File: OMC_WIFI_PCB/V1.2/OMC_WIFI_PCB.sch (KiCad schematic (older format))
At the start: 20 parts, among them J1 Line Input, J10 Power, J11 Conn_01x06_Male, J12 Line Output, J13 Conn_01x06_Male, J2 Nuetral Input, J3 Neutral Output, J4 Switch, J5 Pins_FT232R, J8 Regulador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

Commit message: Actualización PCB y nueva librería para plug macho
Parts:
- removed J1: Line Input, omc-plugs:OMC-Male-Plug, symbol Connector:Conn_01x01_Male
- removed J2: Nuetral Input, omc-plugs:OMC-Male-Plug, symbol Connector:Conn_01x01_Male
- added J1: Conn_01x02_Male, omc-plugs:OMC-Male-Plug, symbol Connector:Conn_01x02_Male
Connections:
- wire segments 105 -> 106
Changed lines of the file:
@@
 	850  2300 850  6000
-$Comp
-L Connector:Conn_01x01_Male J2
-U 1 1 624922FE
-P 1150 1450
-F 0 "J2" H 1258 1631 50  0000 C CNN
-F 1 "Nuetral Input" H 1200 1406 50  0000 C CNN
-F 2 "omc-plugs:OMC-Male-Plug" H 1150 1450 50  0001 C CNN
-F 3 "~" H 1150 1450 50  0001 C CNN
-	1    1150 1450
-	1    0    0    -1
-$EndComp
 $Comp
 L RF_Module:ESP32-WROOM-32 U1
@@
 $EndComp
 $Comp
-L Connector:Conn_01x01_Male J1
-U 1 1 6246AC9C
-P 1150 1150
-F 0 "J1" H 1258 1331 50  0000 C CNN
-F 1 "Line Input" H 1258 1240 50  0000 C CNN
-F 2 "omc-plugs:OMC-Male-Plug" H 1150 1150 50  0001 C CNN
-F 3 "~" H 1150 1150 50  0001 C CNN
-	1    1150 1150
-	1    0    0    -1
-$EndComp
-$Comp
 L power:PWR_FLAG #FLG0103
 U 1 1 62597663
@@
 	1    0    0    -1
 $EndComp
+$Comp
+L Connector:Conn_01x02_Male J1
+U 1 1 62564E0F
+P 1150 1150
+F 0 "J1" H 1258 1331 50  0000 C CNN
+F 1 "Conn_01x02_Male" H 1258 1240 50  0000 C CNN
+F 2 "omc-plugs:OMC-Male-Plug" H 1150 1150 50  0001 C CNN
+F 3 "~" H 1150 1150 50  0001 C CNN
+	1    1150 1150
+	1    0    0    -1
+$EndComp
+Wire Wire Line
+	1350 1250 1350 1450
 $EndSCHEMATC

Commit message: Actualización PCB y Librerías
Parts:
- removed J10: Power, TerminalBlock:TerminalBlock_bornier-4_P5.08mm, symbol Connector:Conn_01x04_Female
- removed J12: Line Output, omc-plugs:OMC-Female-Plug, symbol Connector:Conn_01x01_Female
- removed J3: Neutral Output, omc-plugs:OMC-Female-Plug, symbol Connector:Conn_01x01_Female
- removed J9: Datos, Connector_JST:JST_XH_S4B-XH-A-1_1x04_P2.50mm_Horizontal, symbol Connector:Conn_01x04_Female
- added D2: LED, LED_SMD:LED_0603_1608Metric_Pad1.05x0.95mm_HandSolder, symbol Device:LED
- added J2: Conn_01x02_Female, omc-schematics LE:OMC-Female-Plug, symbol Connector:Conn_01x02_Female
- added R2: 330, Resistor_SMD:R_0603_1608Metric_Pad0.98x0.95mm_HandSolder, symbol Device:R
- added U2: PZEM-004T-100A, omc-schematics LE:PZEM-OO4T-100A, symbol omc-schematics:PZEM-004T-100A
- D1: footprint LED_THT:LED_D3.0mm -> LED_SMD:LED_0603_1608Metric_Pad1.05x0.95mm_HandSolder
- K1: footprint RELAY_SLA-12VDC-SL-C -> SLA-12VDC-SL-C LE:RELAY_SLA-12VDC-SL-C
- R1: footprint Resistor_SMD:R_2010_5025Metric_Pad1.40x2.65mm_HandSolder -> Resistor_SMD:R_0603_1608Metric_Pad0.98x0.95mm_HandSolder
- R3: renamed from R2; footprint Resistor_SMD:R_2010_5025Metric_Pad1.40x2.65mm_HandSolder -> Resistor_SMD:R_0603_1608Metric_Pad0.98x0.95mm_HandSolder
- renumbered D2 to D3
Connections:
- net labels added: D22_LED_G, D23_LED_R
- net labels removed: D23_LED, VN_ZMPT, VP_ACS
- wire segments 106 -> 105
- no-connect marks 29 -> 30
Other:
- note added: "LEDs"
- note added: "Regulador 3V\n"
- note removed: "LED"
- moved on the sheet: J1, J8

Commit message: Actualización PCB
Diseño casi final
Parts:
- added C1: 1u, Capacitor_SMD:C_0603_1608Metric_Pad1.08x0.95mm_HandSolder, symbol Device:C
- added J3: Conn_01x02_Male, Connector_PinHeader_2.54mm:PinHeader_1x02_P2.54mm_Vertical, symbol Connector:Conn_01x02_Male
- added R4: 10k, Resistor_SMD:R_0603_1608Metric_Pad0.98x0.95mm_HandSolder, symbol Device:R
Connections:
- net +3V: now also R4.1; no longer U1.2 (VDD)
- net CTS: now also J5.2 (Pin_2); no longer J5.5 (Pin_5)
- net D22_LED_G: now also D1.2 (A), U1.37 (IO23); no longer R1.1, U1.36 (IO22)
- net D23_LED_R: now also D2.2 (A), U1.36 (IO22); no longer R2.1, U1.37 (IO23)
- net DTR: now also J5.6 (Pin_6); no longer J5.1 (Pin_1)
- net GND: now also J5.1 (Pin_1), R1.2, R2.2, C1.2, J3.1 (Pin_1); no longer D1.1 (K), D2.1 (K), J5.6 (Pin_6)
- net RX0: now also J5.4 (Pin_4); no longer J5.3 (Pin_3)
- net TX0: now also J5.5 (Pin_5); no longer J5.2 (Pin_2)
- net VCC: now also J5.3 (Pin_3); no longer J5.4 (Pin_4)
- net BOOT: no longer names the net of U1.25 (IO0)
- net BOOT: now also J3.2 (Pin_2)
- new net: D1.1 (K), R1.1
- new net: C1.1, R4.2, U1.2 (VDD)
- new net: D2.1 (K), R2.1
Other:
- moved on the sheet: D1, D2, R1, R2
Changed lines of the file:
@@
 L Device:R R1
 U 1 1 620FCE7F
-P 5200 4100
-F 0 "R1" V 5407 4100 50  0000 C CNN
-F 1 "330" V 5316 4100 50  0000 C CNN
-F 2 "Resistor_SMD:R_0603_1608Metric_Pad0.98x0.95mm_HandSolder" V 5130 4100 50  0001 C CNN
-F 3 "~" H 5200 4100 50  0001 C CNN
-	1    5200 4100
+P 5650 4100
+F 0 "R1" V 5857 4100 50  0000 C CNN
+F 1 "330" V 5766 4100 50  0000 C CNN
+F 2 "Resistor_SMD:R_0603_1608Metric_Pad0.98x0.95mm_HandSolder" V 5580 4100 50  0001 C CNN
+F 3 "~" H 5650 4100 50  0001 C CNN
+	1    5650 4100
 	0    -1   -1   0
 $EndComp
@@
 L Device:LED D1
 U 1 1 621083D3
-P 5600 4100
-F 0 "D1" H 5593 4317 50  0000 C CNN
-F 1 "LED" H 5593 4226 50  0000 C CNN
-F 2 "LED_SMD:LED_0603_1608Metric_Pad1.05x0.95mm_HandSolder" H 5600 4100 50  0001 C CNN
-F 3 "~" H 5600 4100 50  0001 C CNN
-	1    5600 4100
+P 5250 4100
+F 0 "D1" H 5243 4317 50  0000 C CNN
+F 1 "LED" H 5243 4226 50  0000 C CNN
+F 2 "LED_SMD:LED_0603_1608Metric_Pad1.05x0.95mm_HandSolder" H 5250 4100 50  0001 C CNN
+F 3 "~" H 5250 4100 50  0001 C CNN
+	1    5250 4100
 	-1   0    0    -1
 $EndComp
-$Comp
-L power:GND #PWR0116
-U 1 1 6210BB6A
-P 5900 4150
-F 0 "#PWR0116" H 5900 3900 50  0001 C CNN
-F 1 "GND" H 5905 3977 50  0000 C CNN
-F 2 "" H 5900 4150 50  0001 C CNN
-F 3 "" H 5900 4150 50  0001 C CNN
-	1    5900 4150
-	1    0    0    -1
-$EndComp
-Wire Wire Line
-	5750 4100 5900 4100
-Wire Wire Line
-	5450 4100 5350 4100
 Text GLabel 4950 4100 0    50   Input ~ 0
 D22_LED_G
-Wire Wire Line
-	4950 4100 5050 4100
 Text Notes 4750 3800 0    50   ~ 10
 LEDs
@@
 L Connector:Conn_01x06_Female J5
 U 1 1 6239A494
-P 5250 2850
-F 0 "J5" H 5278 2826 50  0000 L CNN
-F 1 "Pins_FT232R" H 5278 2735 50  0000 L CNN
-F 2 "Connector_PinSocket_2.54mm:PinSocket_1x06_P2.54mm_Vertical" H 5250 2850 50  0001 C CNN
-F 3 "~" H 5250 2850 50  0001 C CNN
-	1    5250 2850
-	1    0    0    -1
+P 5250 2950
+F 0 "J5" H 5278 2926 50  0000 L CNN
+F 1 "Pins_FT232R" H 5278 2835 50  0000 L CNN
+F 2 "Connector_PinSocket_2.54mm:PinSocket_1x06_P2.54mm_Vertical" H 5250 2950 50  0001 C CNN
+F 3 "~" H 5250 2950 50  0001 C CNN
+	1    5250 2950
+	1    0    0    1
 $EndComp
 Text GLabel 4850 2850 0    50   Input ~ 0
@@
 Wire Wire Line
 	3250 5050 3450 5050
-Text GLabel 3450 2950 2    50   Input ~ 0
-BOOT
 Wire Wire Line
 	1850 4650 2050 4650
@@
 Text GLabel 3450 3050 2    50   Input ~ 0
 TX0
-Text GLabel 3450 4550 2    50   Input ~ 0
+Text GLabel 3450 4450 2    50   Input ~ 0
 D23_LED_R
 Text GLabel 3450 4350 2    50   Input ~ 0
@@
 Wire Wire Line
 	5350 5550 5350 5600
-Text GLabel 2150 2750 0    50   Input ~ 0
+Text GLabel 1100 2750 0    50   Input ~ 0
 +3V
-Wire Wire Line
-	2150 2750 2650 2750
 Wire Wire Line
 	5650 3250 5750 3250
@@
 L Device:R R2
 U 1 1 62628640
-P 5200 4500
-F 0 "R2" V 5407 4500 50  0000 C CNN
-F 1 "330" V 5316 4500 50  0000 C CNN
-F 2 "Resistor_SMD:R_0603_1608Metric_Pad0.98x0.95mm_HandSolder" V 5130 4500 50  0001 C CNN
-F 3 "~" H 5200 4500 50  0001 C CNN
-	1    5200 4500
+P 5650 4500
+F 0 "R2" V 5857 4500 50  0000 C CNN
+F 1 "330" V 5766 4500 50  0000 C CNN
+F 2 "Resistor_SMD:R_0603_1608Metric_Pad0.98x0.95mm_HandSolder" V 5580 4500 50  0001 C CNN
+F 3 "~" H 5650 4500 50  0001 C CNN
+	1    5650 4500
 	0    -1   -1   0
 $EndComp
@@
 L Device:LED D2
 U 1 1 62628646
-P 5600 4500
-F 0 "D2" H 5593 4717 50  0000 C CNN
-F 1 "LED" H 5593 4626 50  0000 C CNN
-F 2 "LED_SMD:LED_0603_1608Metric_Pad1.05x0.95mm_HandSolder" H 5600 4500 50  0001 C CNN
-F 3 "~" H 5600 4500 50  0001 C CNN
-	1    5600 4500
+P 5250 4500
+F 0 "D2" H 5243 4717 50  0000 C CNN
+F 1 "LED" H 5243 4626 50  0000 C CNN
+F 2 "LED_SMD:LED_0603_1608Metric_Pad1.05x0.95mm_HandSolder" H 5250 4500 50  0001 C CNN
+F 3 "~" H 5250 4500 50  0001 C CNN
+	1    5250 4500
 	-1   0    0    -1
 $EndComp
@@
 	1    0    0    -1
 $EndComp
-Wire Wire Line
-	5750 4500 5900 4500
-Wire Wire Line
-	5450 4500 5350 4500
 Text GLabel 4950 4500 0    50   Input ~ 0
 D23_LED_R
-Wire Wire Line
-	4950 4500 5050 4500
 Wire Wire Line
 	5900 4550 5900 4500
 Text Notes 4600 5750 0    50   ~ 10
 Regulador 3V\n
-Text GLabel 3450 4450 2    50   Input ~ 0
+Text GLabel 3450 4550 2    50   Input ~ 0
 D22_LED_G
 Wire Notes Line
@@
 	1    0    0    1
 $EndComp
+$Comp
+L power:GND #PWR0116
+U 1 1 6210BB6A
+P 5900 4150
+F 0 "#PWR0116" H 5900 3900 50  0001 C CNN
+F 1 "GND" H 5905 3977 50  0000 C CNN
+F 2 "" H 5900 4150 50  0001 C CNN
+F 3 "" H 5900 4150 50  0001 C CNN
+	1    5900 4150
+	1    0    0    -1
+$EndComp
+Wire Wire Line
+	5400 4100 5500 4100
+Wire Wire Line
+	5100 4100 4950 4100
+Wire Wire Line
+	5100 4500 4950 4500
+Wire Wire Line
+	5400 4500 5500 4500
+Wire Wire Line
+	5800 4100 5900 4100
+Wire Wire Line
+	5800 4500 5900 4500
+$Comp
+L Device:R R4
+U 1 1 626E4FB2
+P 1300 2750
+F 0 "R4" V 1507 2750 50  0000 C CNN
+F 1 "10k" V 1416 2750 50  0000 C CNN
+F 2 "Resistor_SMD:R_0603_1608Metric_Pad0.98x0.95mm_HandSolder" V 1230 2750 50  0001 C CNN
+F 3 "~" H 1300 2750 50  0001 C CNN
+	1    1300 2750
+	0    -1   -1   0
+$EndComp
+$Comp
+L Device:C C1
+U 1 1 626F2827
+P 1500 2950
+F 0 "C1" H 1615 2996 50  0000 L CNN
+F 1 "1u" H 1615 2905 50  0000 L CNN
+F 2 "Capacitor_SMD:C_0603_1608Metric_Pad1.08x0.95mm_HandSolder" H 1538 2800 50  0001 C CNN
+F 3 "~" H 1500 2950 50  0001 C CNN
+	1    1500 2950
+	1    0    0    -1
+$EndComp
+Wire Wire Line
+	1100 2750 1150 2750
+Wire Wire Line
+	1450 2750 1500 2750
+Wire Wire Line
+	1500 2800 1500 2750
+Connection ~ 1500 2750
+Wire Wire Line
+	1500 2750 2650 2750
+$Comp
+L power:GND #PWR0117
+U 1 1 627210BC
+P 1500 3100
+F 0 "#PWR0117" H 1500 2850 50  0001 C CNN
+F 1 "GND" H 1505 2927 50  0000 C CNN
+F 2 "" H 1500 3100 50  0001 C CNN
+F 3 "" H 1500 3100 50  0001 C CNN
+	1    1500 3100
+	1    0    0    -1
+$EndComp
+$Comp
+L Connector:Conn_01x02_Male J3
+U 1 1 62727A97
+P 3550 2750
+F 0 "J3" V 3612 2794 50  0000 L CNN
+F 1 "Conn_01x02_Male" V 3703 2794 50  0000 L CNN
+F 2 "Connector_PinHeader_2.54mm:PinHeader_1x02_P2.54mm_Vertical" H 3550 2750 50  0001 C CNN
+F 3 "~" H 3550 2750 50  0001 C CNN
+	1    3550 2750
+	0    1    1    0
+$EndComp
+$Comp
+L power:GND #PWR0118
+U 1 1 6275F063
+P 3950 3000
+F 0 "#PWR0118" H 3950 2750 50  0001 C CNN
+F 1 "GND" H 3955 2827 50  0000 C CNN
+F 2 "" H 3950 3000 50  0001 C CNN
+F 3 "" H 3950 3000 50  0001 C CNN
+	1    3950 3000
+	1    0    0    -1
+$EndComp
+Wire Wire Line
+	3950 2950 3950 3000
+Wire Wire Line
+	3550 2950 3950 2950
 $EndSCHEMATC

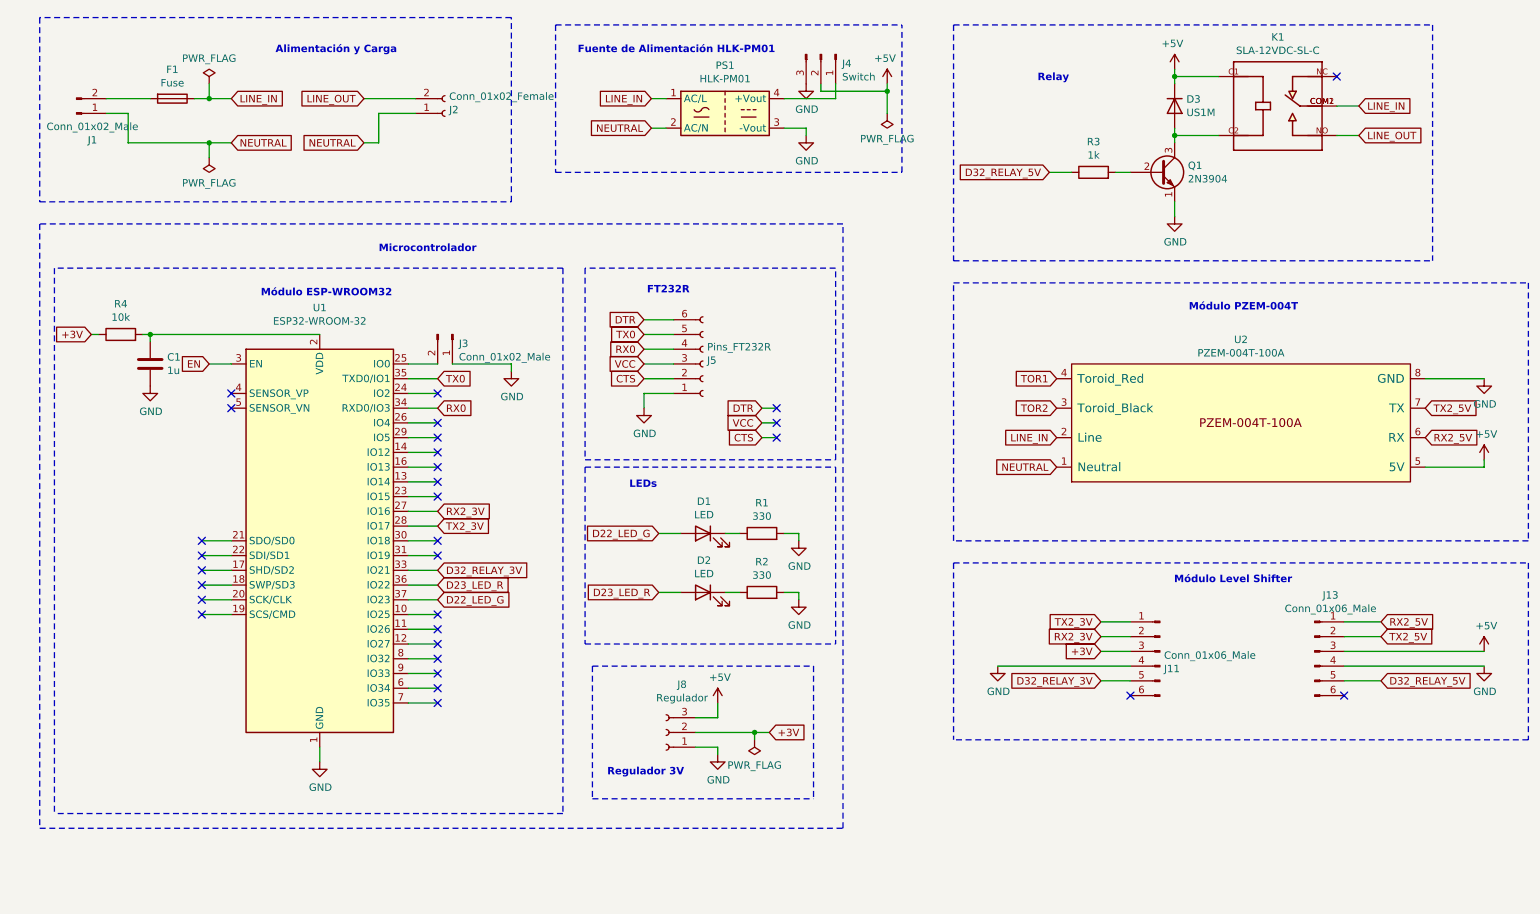
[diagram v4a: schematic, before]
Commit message: Modelos 3D de clavijas
+Creación de modelos 3D para Clavijas
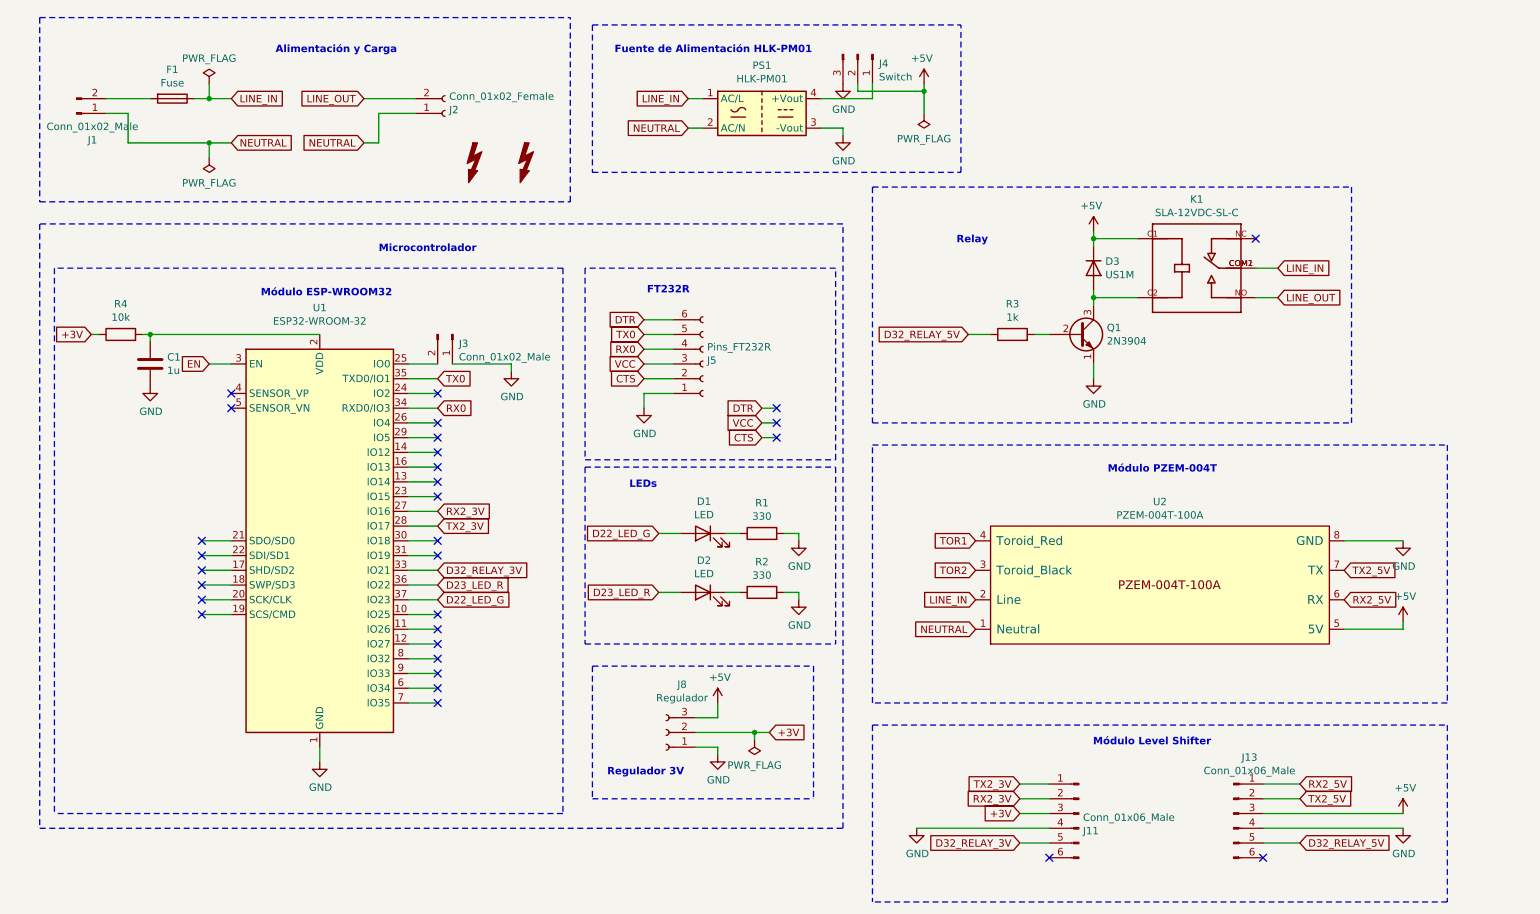
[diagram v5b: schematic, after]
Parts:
- added SYM1, SYM2: SYM_Flash_Small, Symbol:Symbol_HighVoltage_Type2_CopperTop_VerySmall, symbol Graphic:SYM_Flash_Small
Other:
- moved on the sheet: D3, J11, J13, J4, K1, PS1, Q1, R3, U2
